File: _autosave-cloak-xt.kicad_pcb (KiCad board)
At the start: 2 copper layers, 289.7 x 98 mm, 168 parts, among them J1 JST, Q1 Q_PMOS_GSD, Q2 Q_PMOS_GSD, U1 STM32F072CBT6, U3 XC6206PxxxMR-Regulator_Linear

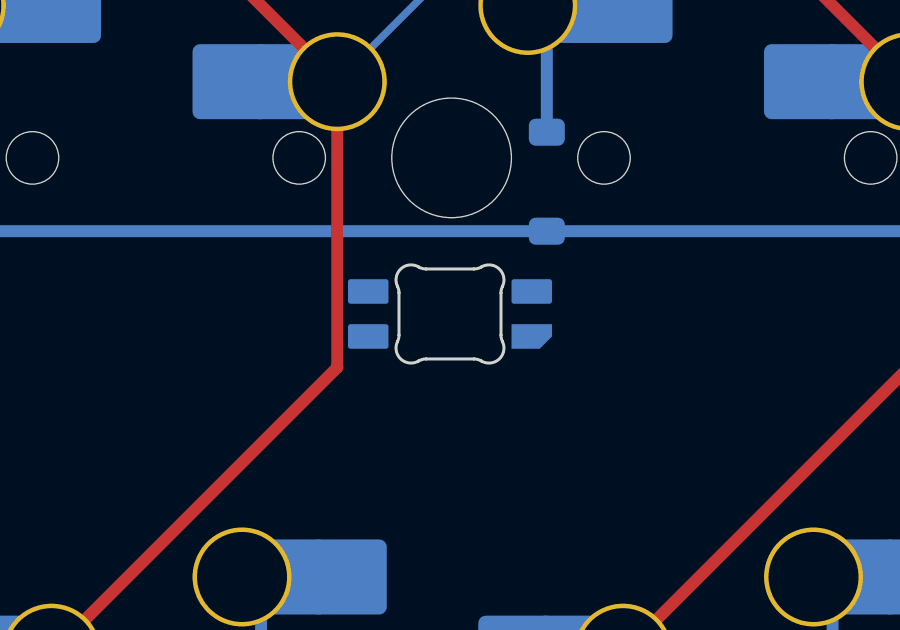
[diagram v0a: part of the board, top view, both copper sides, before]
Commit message: Add schematics for RGB lighting
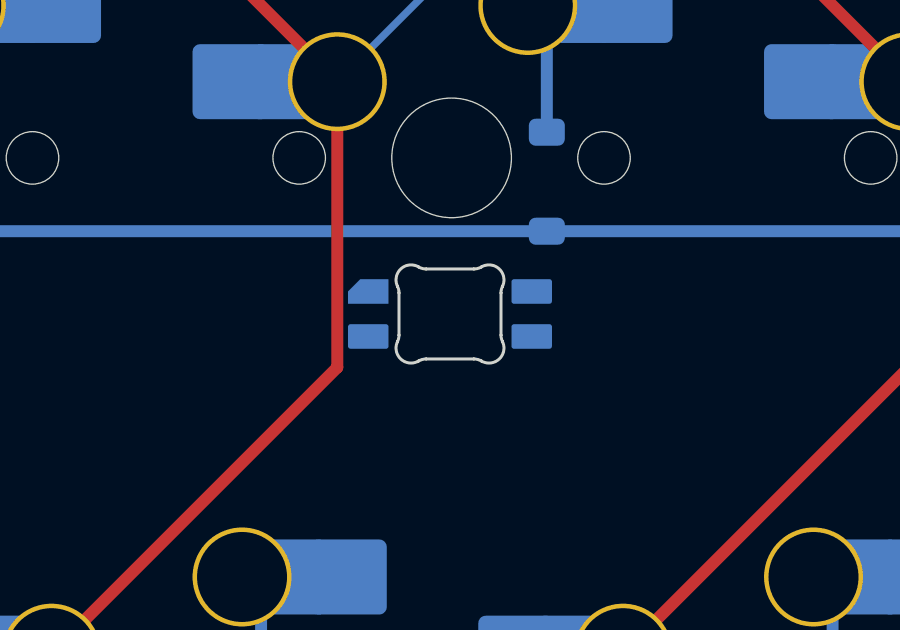
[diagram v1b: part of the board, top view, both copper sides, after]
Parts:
- LED3: footprint PCM_marbastlib-mx:LED_MX_6028R -> PCM_marbastlib-mx:LED_MX_6028R-ROT
